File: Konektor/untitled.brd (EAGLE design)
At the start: 118 x 63 mm, 11 parts, among them J1 RJ45-8N-B, J2 RJ45-8N-B, X1 C-GRID-02-70543, X2 C-GRID-05-70543

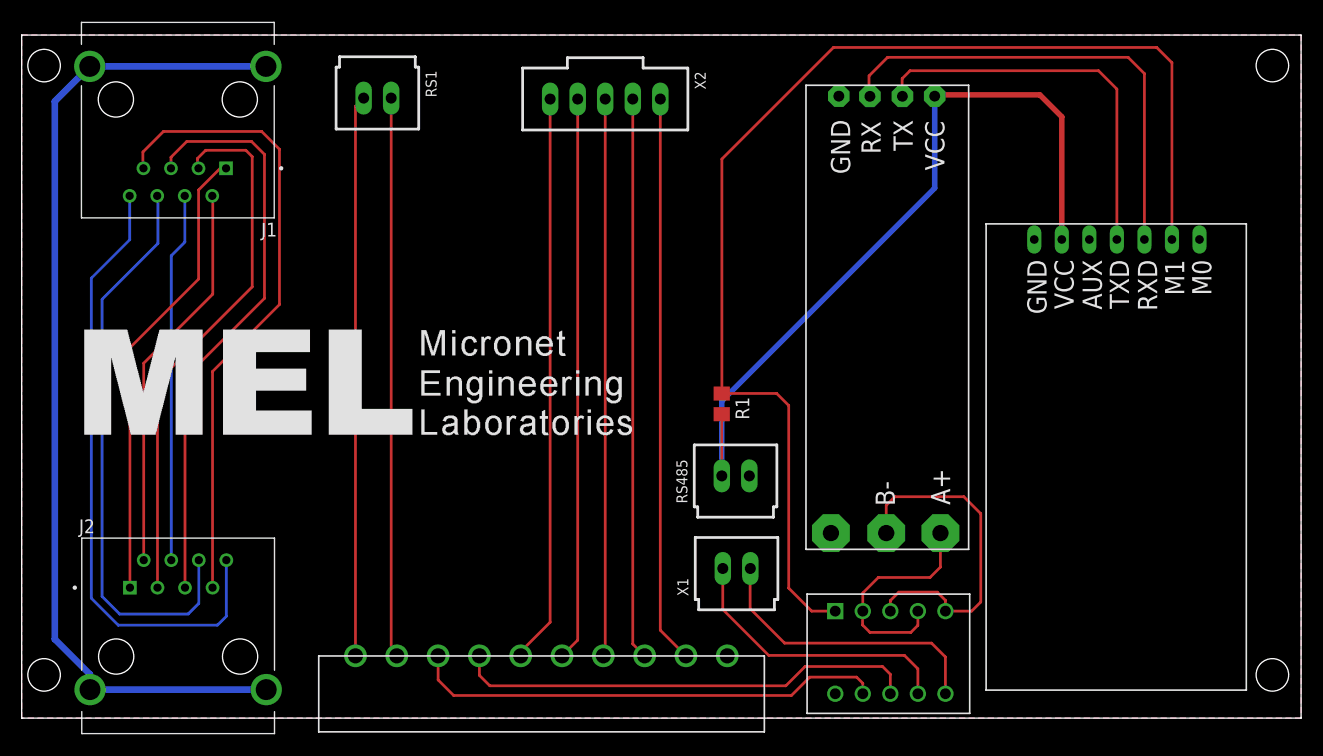
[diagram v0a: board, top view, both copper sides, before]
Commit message: REVISI PCB Konektor
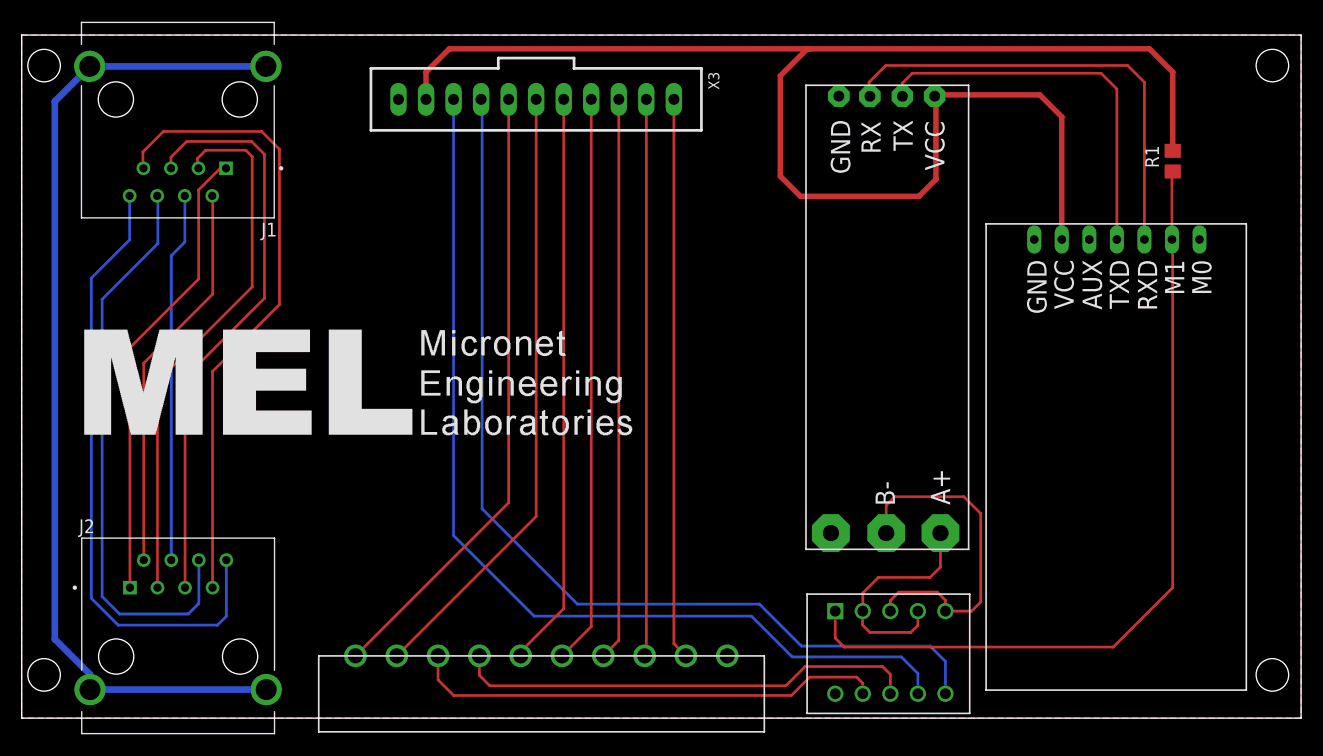
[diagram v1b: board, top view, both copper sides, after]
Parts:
- removed RS1, RS485, X1: C-GRID-02-70543, con-molex:70543-02
- removed X2: C-GRID-05-70543, con-molex:70543-05
- added X3: C-GRID-11-70543, con-molex:70543-11
- moved R1 47.2 mm to (106.2, 51.4), turned to 90 degrees
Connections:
- removed net N$5: DP-05RP1.P$9, X1.1
- removed net N$6: DP-05RP1.P$10, X1.2
- new net A2: DP-05RP1.P$9, X3.9
- new net B2: DP-05RP1.P$10, X3.8
- net 5V: now also X3.10; no longer RS485.1
- net GND: now also X3.11; no longer RS485.2
- net N$1: now also X3.7; no longer RS1.2
- net N$15: now also X3.4; no longer X2.4
- net N$16: now also X3.3; no longer X2.3
- net N$17: now also X3.2; no longer X2.2
- net N$18: now also X3.1; no longer X2.1
- net N$2: now also X3.6; no longer RS1.1
- net N$7: now also X3.5; no longer X2.5
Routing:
- net A2: track 0.00 -> 90.2 mm
- net B2: track 0.00 -> 89.4 mm
- net 5V: track 72.8 -> 140.7 mm
- net M1: track 112.9 -> 74.7 mm
- net N$6: track 27.0 -> 0.00 mm
- net N$5: track 26.3 -> 0.00 mm
- net N$1: track 51.8 -> 57.2 mm
- net N$2: track 51.7 -> 56.6 mm
- net N$3: track 44.0 -> 42.5 mm
- net N$16: track 51.4 -> 52.2 mm
- net N$18: track 52.3 -> 51.8 mm
